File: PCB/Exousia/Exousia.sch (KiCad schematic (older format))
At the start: 3 parts

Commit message: added more stuff
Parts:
- added C? (x7): C, symbol Device:C
- added C? (x2): CP1, symbol Device:CP1
- added J?: I2C buss, symbol Connector:Conn_01x04_Female
- added L?: L, symbol Device:L
- added Q? (x4): Q_NMOS_DGS, symbol Device:Q_NMOS_DGS
- added R? (x2): 20m, symbol Device:R
- added R? (x8): R, symbol Device:R
- added R? (x4): 3.3K, symbol Device:R
- added TP?: FRWPG, symbol Connector:TestPoint
- added TP?: RVSPG, symbol Connector:TestPoint
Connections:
- net GND: now reaches J?.1 (Pin_1)
- net GND: now also J?.1 (Pin_1), U?.25 (ADDR0), U?.32 (ADDR1), C?.2, C?.2, C?.2, C?.2, C?.2, J?.1 (Pin_1), Q?.3 (S), Q?.3 (S), R?.1, R?.1
- net at J?.2 (Pin_2): now also U?.13 (ADPS), R?.2, R?.2, R?.2
- net at J?.2 (Pin_2): now also C?.1, C?.1, R?.1, R?.2, R?.2
- net at U?.1 (CSON): now also C?.1, R?.1
- net at U?.10 (PHASE1): now also C?.1, L?.1, Q?.1 (D), Q?.3 (S)
- net at U?.11 (UGATE1): now also Q?.2 (G)
- net at U?.12 (BOOT1): now also C?.2
- net at U?.14 (CSIN): now also C?.1, R?.1
- net at U?.15 (CSIP): now also C?.2, R?.1
- net at U?.16 (ADP): now also R?.1, R?.2
- net at U?.2 (CSOP): now also C?.2, R?.1
- net SDA: now reaches U?.21 (SDA)
- net SDA: now also J?.3 (Pin_3), R?.2
- net SCL: now reaches U?.22 (SCL)
- net SCL: now also J?.2 (Pin_2), R?.2
- net at U?.24 (FRWPG): now also R?.2, TP?.1
- net at U?.26 (RVSPG): now also R?.2, TP?.1
- net at U?.29 (REF): now also C?.1
- net at U?.3 (VOUTS): now also R?.1, R?.2
- net at U?.31 (VOUT): now also Q?.1 (D), R?.2, R?.2
- net at U?.4 (BOOT2): now also C?.2
- net at U?.5 (UGATE2): now also Q?.2 (G)
- net at U?.6 (PHASE2): now also C?.1, L?.2, Q?.1 (D), Q?.3 (S)
- net at U?.7 (LGATE2): now also Q?.2 (G)
- net at U?.9 (LGATE1): now also Q?.2 (G)
- new net: C?.1, C?.1, Q?.1 (D), R?.1, R?.2
- new net +3V3: J?.4 (Pin_4), R?.1, R?.1, R?.1, R?.1
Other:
- moved on the sheet: J?

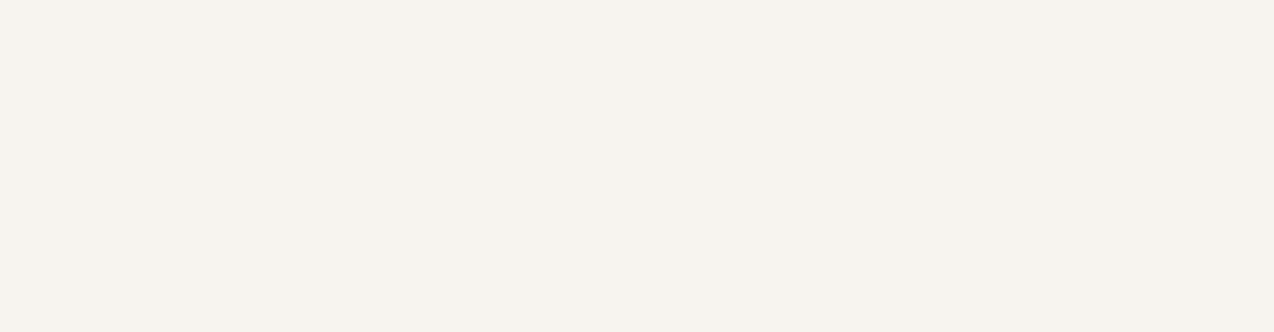
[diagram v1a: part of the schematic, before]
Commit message: added refrence design files
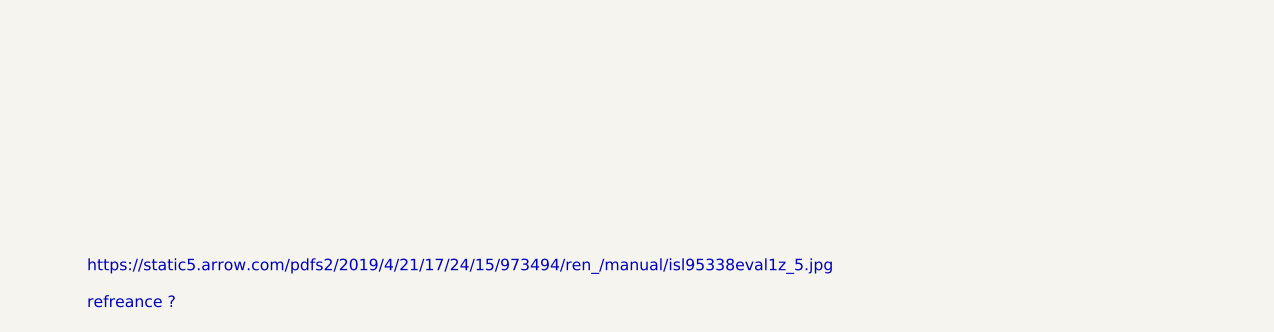
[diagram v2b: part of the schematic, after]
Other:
- note added: "https://static5.arrow.com/pdfs2/2019/4/21/17/24/15/973494/ren_/manual/isl95338eval1z_5.jpg\n\nrefreance ?"
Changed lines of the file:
@@
 Wire Wire Line
 	9300 1350 9350 1350
+Text Notes 1400 6900 0    50   ~ 0
+https://static5.arrow.com/pdfs2/2019/4/21/17/24/15/973494/ren_/manual/isl95338eval1z_5.jpg\n\nrefreance ?
 $EndSCHEMATC

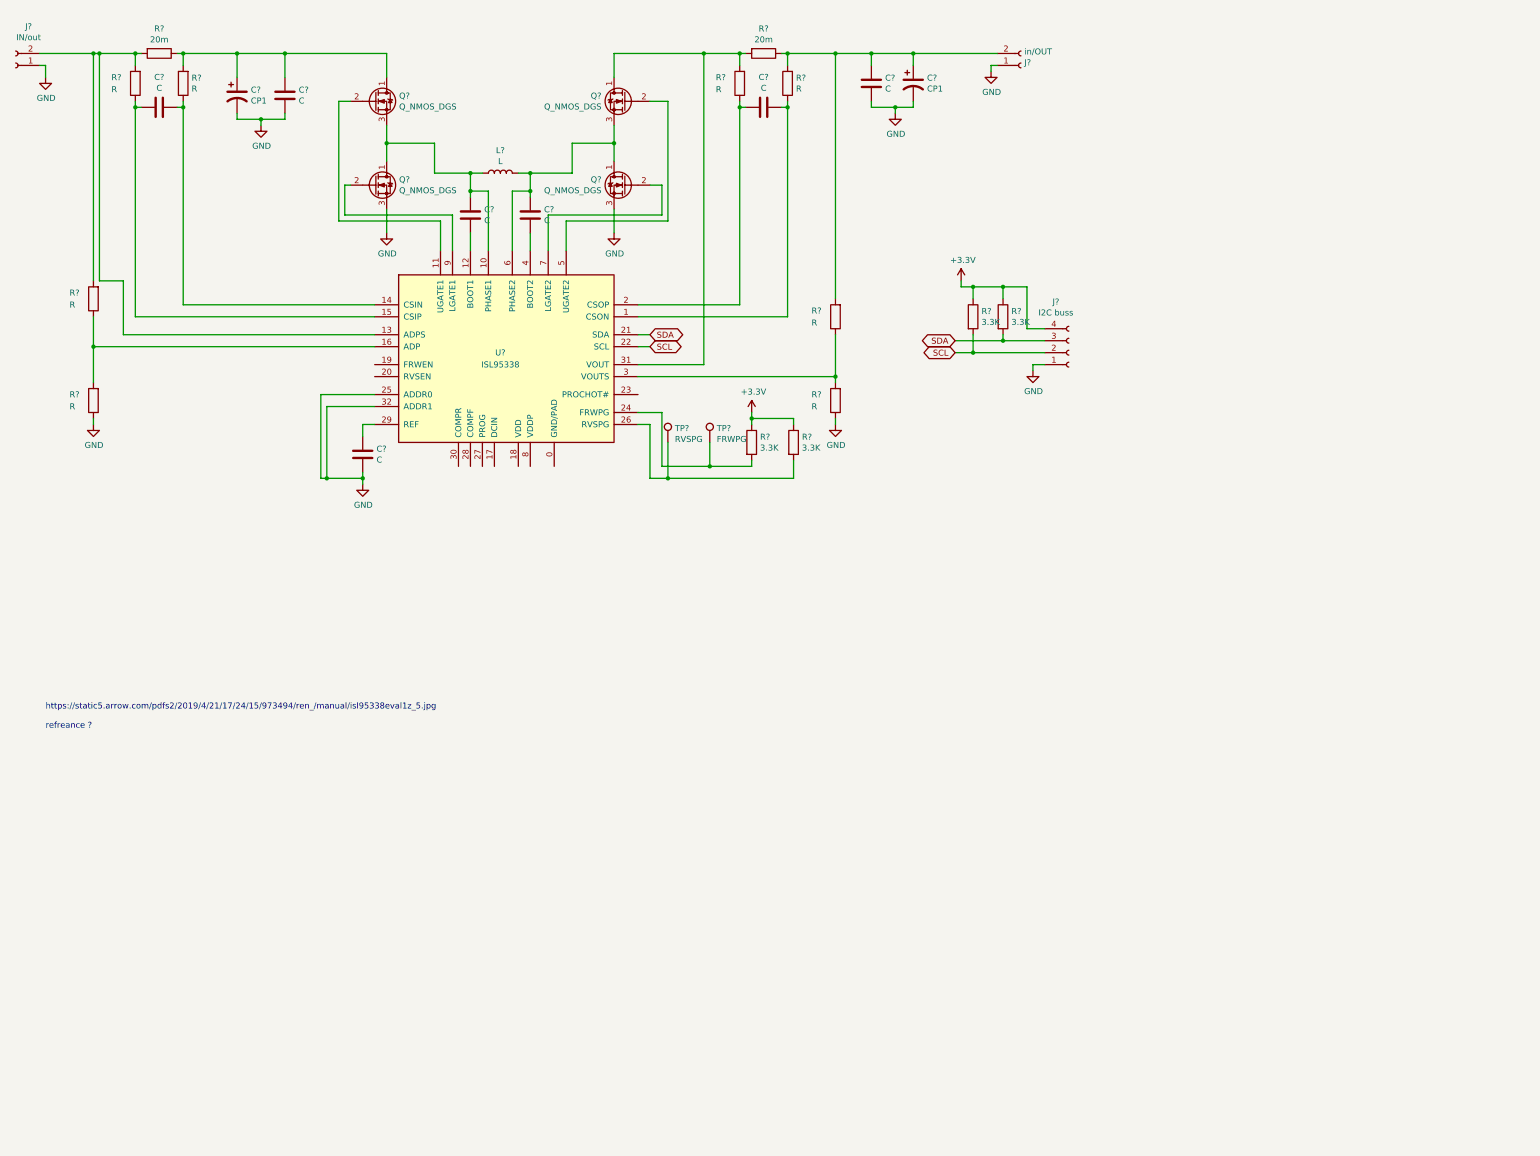
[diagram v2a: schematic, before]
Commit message: added nice FETs and more detailed circuti diogram
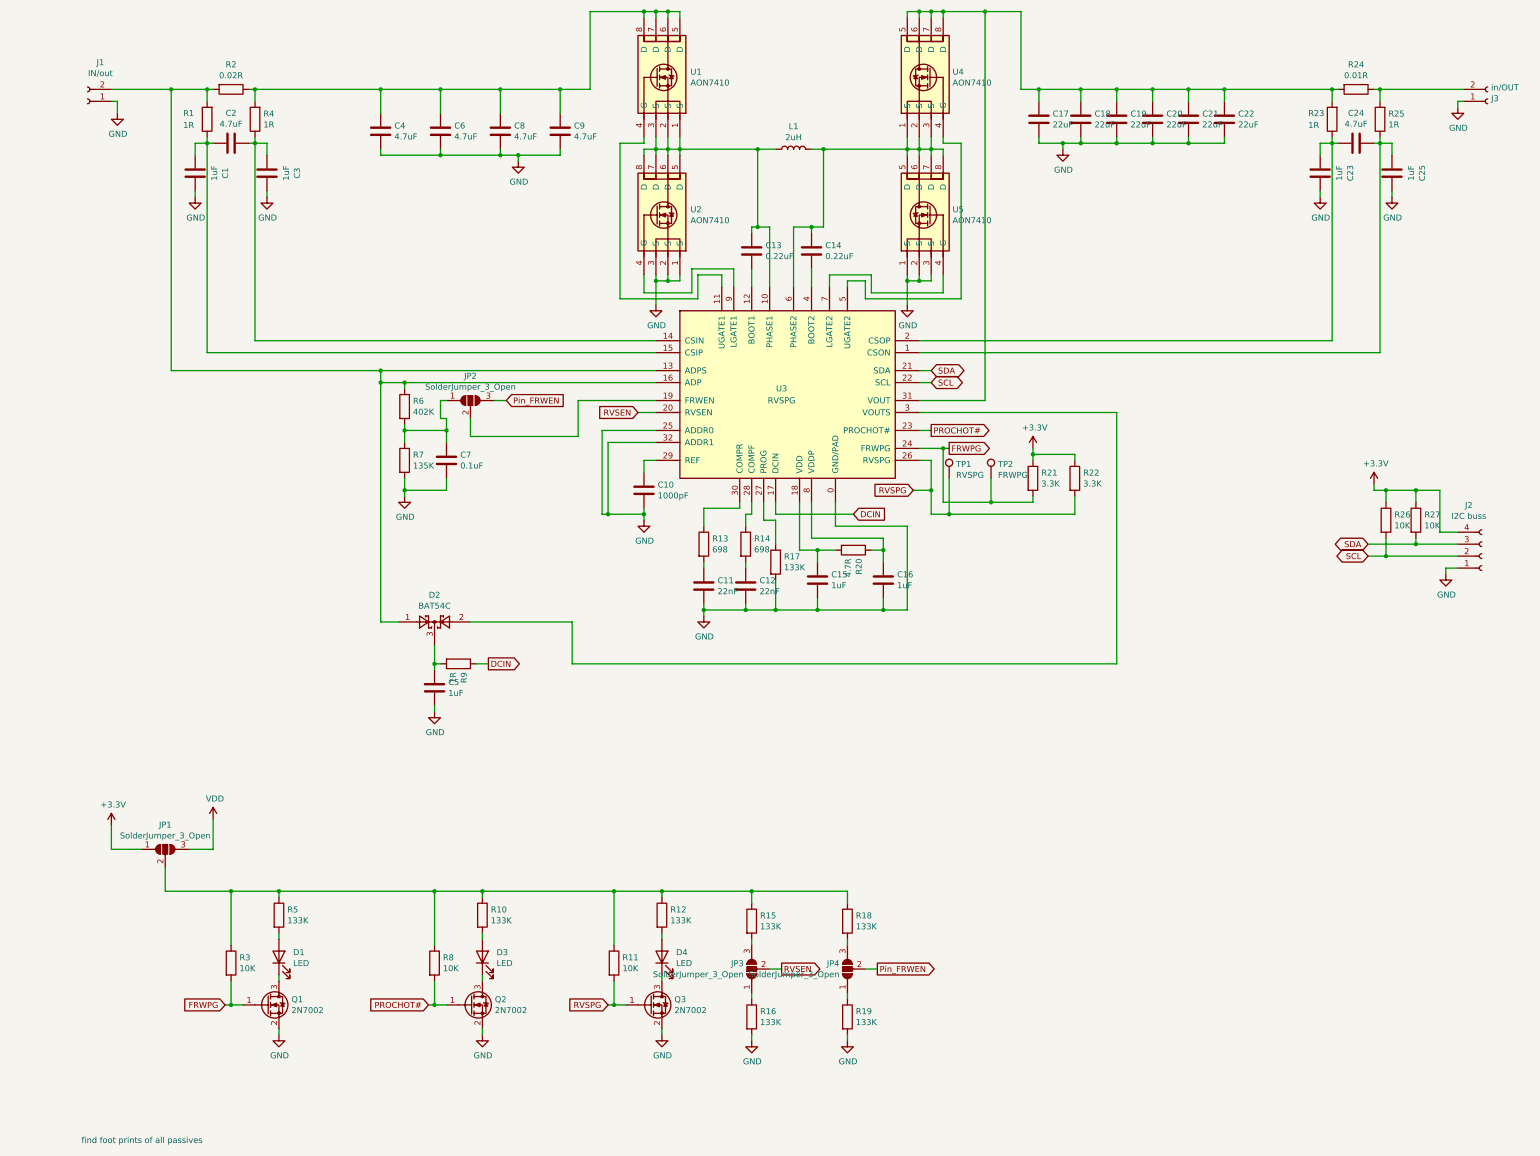
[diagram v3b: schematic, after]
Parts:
- removed C?: C, symbol Device:C
- removed C? (x2): CP1, symbol Device:CP1
- removed Q? (x4): Q_NMOS_DGS, symbol Device:Q_NMOS_DGS
- removed R? (x4): R, symbol Device:R
- added C1, C15, C16, C23, C25, C3, C5: 1uF, symbol Device:C
- added C11, C12: 22nF, symbol Device:C
- added C18, C19, C20, C21, C22: 22uF, symbol Device:C
- added C4, C6, C8, C9: 4.7uF, symbol Device:C
- added C7: 0.1uF, symbol Device:C
- added D1, D3, D4: LED, symbol Device:LED
- added D2: BAT54C, Package_TO_SOT_SMD:SOT-23, symbol Diode:BAT54C
- added JP1, JP2, JP3, JP4: SolderJumper_3_Open, symbol Jumper:SolderJumper_3_Open
- added Q1, Q2, Q3: 2N7002, Package_TO_SOT_SMD:SOT-23, symbol Transistor_FET:2N7002
- added R10, R12, R15, R16, R17, R18, R19, R5: 133K, symbol Device:R
- added R11, R3, R8: 10K, symbol Device:R
- added R13, R14: 698, symbol Device:R
- added R20: 4.7R, symbol Device:R
- added R6: 402K, symbol Device:R
- added R7: 135K, symbol Device:R
- added R9: 1R, symbol Device:R
- added U1, U2, U4, U5: AON7410, Package_DFN_QFN:DFN-6-1EP_3x3mm_P1mm_EP1.5x2.4mm, symbol AON7410:AON7410
- C10: renamed from C?; value C -> 1000pF
- C13, C14: renamed from C?; value C -> 0.22uF
- C17: renamed from C?; value C -> 22uF
- C2, C24: renamed from C?; value C -> 4.7uF
- L1: renamed from L?; value L -> 2uH
- R1, R23, R25, R4: renamed from R?; value R -> 1R
- R2: renamed from R?; value 20m -> 0.02R
- R24: renamed from R?; value 20m -> 0.01R
- R26, R27: renamed from R?; value 3.3K -> 10K
- U3: renamed from U?; value ISL95338 -> RVSPG
- gave numbers to parts that had none: 7
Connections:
- net +3V3: now also JP1.1 (A)
- net GND: now also U3.0 (GND/PAD), C1.1, C11.2, C12.2, C15.2, C16.2, C18.2, C19.2, C20.2, C21.2, C22.2, C23.1, C25.1, C3.1, C4.2, C5.2, C6.2, C7.2, C8.2, C9.2, Q1.2 (S), Q2.2 (S), Q3.2 (S), R16.2, R17.2, R19.2, R7.2, U2.1 (S), U2.2 (S), U2.3 (S), U5.1 (S), U5.2 (S), U5.3 (S)
- net at J1.2 (Pin_2), R1.2, R2.2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: now also U3.16 (ADP), D2.1, R6.1
- net at J3.2 (Pin_2), R24.1, R25.2: no longer C17.1
- net at C24.1, R25.1, U3.1 (CSON): now also C25.2
- net at C13.1, L1.1, U3.10 (PHASE1): now also U1.1 (S), U1.2 (S), U1.3 (S), U2.5 (D), U2.6 (D), U2.7 (D), U2.8 (D)
- net at U3.11 (UGATE1): now also U1.4 (G)
- net at C2.1, R4.1, U3.14 (CSIN): now also C3.2
- net at C2.2, R1.1, U3.15 (CSIP): now also C1.2
- net DCIN: now reaches U3.17 (DCIN)
- net DCIN: now also R9.1
- net at U3.18 (VDD): now also C15.1, R20.2
- net at U3.19 (FRWEN): now also JP2.2 (C)
- net at C24.2, R23.1, U3.2 (CSOP): now also C23.2
- net RVSEN: now reaches U3.20 (RVSEN)
- net RVSEN: now also JP3.2 (C)
- net PROCHOT#: now reaches U3.23 (PROCHOT#)
- net PROCHOT#: now also Q2.1 (G), R8.2
- net FRWPG: now reaches R21.2, TP2.1, U3.24 (FRWPG)
- net FRWPG: now also Q1.1 (G), R3.2
- net RVSPG: now reaches R22.2, TP1.1, U3.26 (RVSPG)
- net RVSPG: now also Q3.1 (G), R11.2
- net at U3.27 (PROG): now also R17.1
- net at U3.28 (COMPF): now also R14.1
- net at U3.3 (VOUTS): now also D2.2
- net at U3.30 (COMPR): now also R13.1
- net at R23.2, R24.2, U3.31 (VOUT): now also C17.1, C18.1, C19.1, C20.1, C21.1, C22.1, U4.5 (D), U4.6 (D), U4.7 (D), U4.8 (D)
- net at U3.5 (UGATE2): now also U4.4 (G)
- net at C14.1, L1.2, U3.6 (PHASE2): now also U4.1 (S), U4.2 (S), U4.3 (S), U5.5 (D), U5.6 (D), U5.7 (D), U5.8 (D)
- net at U3.7 (LGATE2): now also U5.4 (G)
- net at U3.8 (VDDP): now also C16.1, R20.1
- net at U3.9 (LGATE1): now also U2.4 (G)
- net at R2.1, R4.2: now also C4.1, C6.1, C8.1, C9.1, U1.5 (D), U1.6 (D), U1.7 (D), U1.8 (D)
- new net: C11.1, R13.2
- new net: C12.1, R14.2
- new net: D1.1 (K), Q1.3 (D)
- new net: D1.2 (A), R5.2
- new net: JP1.2 (C), R10.1, R11.1, R12.1, R15.1, R18.1, R3.1, R5.1, R8.1
- new net: D3.1 (K), Q2.3 (D)
- new net: D3.2 (A), R10.2
- new net: D4.1 (K), Q3.3 (D)
- new net: D4.2 (A), R12.2
- new net: C5.1, D2.3, R9.2
- new net: C7.1, JP2.1 (A), R6.2, R7.1
- new net: JP3.1 (A), R16.1
- new net: JP3.3 (B), R15.2
- new net: JP4.1 (A), R19.1
- new net: JP4.3 (B), R18.2
- new net Pin_FRWEN: JP2.3 (B), JP4.2 (C)
- new net VDD: JP1.3 (B)
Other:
- note added: "find foot prints of all passives \n\n"
- note removed: "https://static5.arrow.com/pdfs2/2019/4/21/17/24/15/973494/ren_/manual/isl95338eval1z_5.jpg\n\nrefreance ?"
- moved on the sheet: C10, C13, C14, C17, C2, C24, J1, J2, J3, L1, R1, R2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

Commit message: started adding footprints to all the components!
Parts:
- C1, C10, C11, C12, C13, C14, C15, C16, C2, C3: footprint (none) -> Capacitor_SMD:C_0603_1608Metric
- C17, C4, C6, C8, C9: footprint (none) -> Capacitor_SMD:C_0805_2012Metric
- R26, R27: footprint (none) -> Resistor_SMD:R_0603_1608Metric
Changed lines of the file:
@@
 F 0 "C10" H 6515 4946 50  0000 L CNN
 F 1 "1000pF" H 6515 4855 50  0000 L CNN
-F 2 "" H 6438 4750 50  0001 C CNN
+F 2 "Capacitor_SMD:C_0603_1608Metric" H 6438 4750 50  0001 C CNN
 F 3 "~" H 6400 4900 50  0001 C CNN
 	1    6400 4900
@@
 F 0 "C13" H 7415 2946 50  0000 L CNN
 F 1 "0.22uF" H 7415 2855 50  0000 L CNN
-F 2 "" H 7338 2750 50  0001 C CNN
+F 2 "Capacitor_SMD:C_0603_1608Metric" H 7338 2750 50  0001 C CNN
 F 3 "~" H 7300 2900 50  0001 C CNN
 	1    7300 2900
@@
 F 0 "C14" H 7915 2946 50  0000 L CNN
 F 1 "0.22uF" H 7915 2855 50  0000 L CNN
-F 2 "" H 7838 2750 50  0001 C CNN
+F 2 "Capacitor_SMD:C_0603_1608Metric" H 7838 2750 50  0001 C CNN
 F 3 "~" H 7800 2900 50  0001 C CNN
 	1    7800 2900
@@
 F 0 "C17" H 9815 1846 50  0000 L CNN
 F 1 "22uF" H 9815 1755 50  0000 L CNN
-F 2 "" H 9738 1650 50  0001 C CNN
+F 2 "Capacitor_SMD:C_0805_2012Metric" H 9738 1650 50  0001 C CNN
 F 3 "~" H 9700 1800 50  0001 C CNN
 	1    9700 1800
@@
 F 0 "C2" V 2698 2000 50  0000 C CNN
 F 1 "4.7uF" V 2789 2000 50  0000 C CNN
-F 2 "" H 2988 1850 50  0001 C CNN
+F 2 "Capacitor_SMD:C_0603_1608Metric" H 2988 1850 50  0001 C CNN
 F 3 "~" H 2950 2000 50  0001 C CNN
 	1    2950 2000
@@
 F 0 "R27" H 12920 5196 50  0000 L CNN
 F 1 "10K" H 12920 5105 50  0000 L CNN
-F 2 "" V 12780 5150 50  0001 C CNN
+F 2 "Resistor_SMD:R_0603_1608Metric" V 12780 5150 50  0001 C CNN
 F 3 "~" H 12850 5150 50  0001 C CNN
 	1    12850 5150
@@
 F 0 "R26" H 12670 5196 50  0000 L CNN
 F 1 "10K" H 12670 5105 50  0000 L CNN
-F 2 "" V 12530 5150 50  0001 C CNN
+F 2 "Resistor_SMD:R_0603_1608Metric" V 12530 5150 50  0001 C CNN
 F 3 "~" H 12600 5150 50  0001 C CNN
 	1    12600 5150
@@
 F 0 "C4" H 4315 1946 50  0000 L CNN
 F 1 "4.7uF" H 4315 1855 50  0000 L CNN
-F 2 "" H 4238 1750 50  0001 C CNN
+F 2 "Capacitor_SMD:C_0805_2012Metric" H 4238 1750 50  0001 C CNN
 F 3 "~" H 4200 1900 50  0001 C CNN
 	1    4200 1900
@@
 F 0 "C6" H 4815 1946 50  0000 L CNN
 F 1 "4.7uF" H 4815 1855 50  0000 L CNN
-F 2 "" H 4738 1750 50  0001 C CNN
+F 2 "Capacitor_SMD:C_0805_2012Metric" H 4738 1750 50  0001 C CNN
 F 3 "~" H 4700 1900 50  0001 C CNN
 	1    4700 1900
@@
 F 0 "C8" H 5315 1946 50  0000 L CNN
 F 1 "4.7uF" H 5315 1855 50  0000 L CNN
-F 2 "" H 5238 1750 50  0001 C CNN
+F 2 "Capacitor_SMD:C_0805_2012Metric" H 5238 1750 50  0001 C CNN
 F 3 "~" H 5200 1900 50  0001 C CNN
 	1    5200 1900
@@
 F 0 "C9" H 5815 1946 50  0000 L CNN
 F 1 "4.7uF" H 5815 1855 50  0000 L CNN
-F 2 "" H 5738 1750 50  0001 C CNN
+F 2 "Capacitor_SMD:C_0805_2012Metric" H 5738 1750 50  0001 C CNN
 F 3 "~" H 5700 1900 50  0001 C CNN
 	1    5700 1900
@@
 F 0 "C3" V 2998 2250 50  0000 C CNN
 F 1 "1uF" V 3089 2250 50  0000 C CNN
-F 2 "" H 3288 2100 50  0001 C CNN
+F 2 "Capacitor_SMD:C_0603_1608Metric" H 3288 2100 50  0001 C CNN
 F 3 "~" H 3250 2250 50  0001 C CNN
 	1    3250 2250
@@
 F 0 "C1" V 2398 2250 50  0000 C CNN
 F 1 "1uF" V 2489 2250 50  0000 C CNN
-F 2 "" H 2688 2100 50  0001 C CNN
+F 2 "Capacitor_SMD:C_0603_1608Metric" H 2688 2100 50  0001 C CNN
 F 3 "~" H 2650 2250 50  0001 C CNN
 	1    2650 2250
@@
 F 0 "C11" H 7015 5746 50  0000 L CNN
 F 1 "22nF" H 7015 5655 50  0000 L CNN
-F 2 "" H 6938 5550 50  0001 C CNN
+F 2 "Capacitor_SMD:C_0603_1608Metric" H 6938 5550 50  0001 C CNN
 F 3 "~" H 6900 5700 50  0001 C CNN
 	1    6900 5700
@@
 F 0 "C12" H 7365 5746 50  0000 L CNN
 F 1 "22nF" H 7365 5655 50  0000 L CNN
-F 2 "" H 7288 5550 50  0001 C CNN
+F 2 "Capacitor_SMD:C_0603_1608Metric" H 7288 5550 50  0001 C CNN
 F 3 "~" H 7250 5700 50  0001 C CNN
 	1    7250 5700
@@
 F 0 "C15" H 7965 5696 50  0000 L CNN
 F 1 "1uF" H 7965 5605 50  0000 L CNN
-F 2 "" H 7888 5500 50  0001 C CNN
+F 2 "Capacitor_SMD:C_0603_1608Metric" H 7888 5500 50  0001 C CNN
 F 3 "~" H 7850 5650 50  0001 C CNN
 	1    7850 5650
@@
 F 0 "C16" H 8515 5696 50  0000 L CNN
 F 1 "1uF" H 8515 5605 50  0000 L CNN
-F 2 "" H 8438 5500 50  0001 C CNN
+F 2 "Capacitor_SMD:C_0603_1608Metric" H 8438 5500 50  0001 C CNN
 F 3 "~" H 8400 5650 50  0001 C CNN
 	1    8400 5650

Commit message: done all but 1 footprints
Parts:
- C18, C19, C20, C21, C22: footprint (none) -> Capacitor_SMD:C_0805_2012Metric
- C23, C24, C25, C5, C7: footprint (none) -> Capacitor_SMD:C_0603_1608Metric
- D1, D3, D4: footprint (none) -> LED_SMD:LED_1206_3216Metric
- J1, J2: footprint (none) -> Connector_PinSocket_2.54mm:PinSocket_1x04_P2.54mm_Vertical
- J3: footprint (none) -> Connector_PinSocket_2.54mm:PinSocket_1x02_P2.54mm_Vertical
- JP1, JP2, JP3, JP4: footprint (none) -> Connector_PinSocket_2.54mm:PinSocket_1x03_P2.54mm_Vertical
- R1, R10, R11, R12, R13, R14, R15, R16, R17, R18, R19, R20, R21, R22, R23, R25, R3, R4, R5, R6, R7, R8, R9: footprint (none) -> Resistor_SMD:R_0603_1608Metric
- R2, R24: footprint (none) -> Resistor_SMD:R_1206_3216Metric
- TP1, TP2: footprint (none) -> TestPoint:TestPoint_Loop_D2.50mm_Drill1.0mm
- U3: footprint (none) -> Package_DFN_QFN:TQFN-24-1EP_4x4mm_P0.5mm_EP2.8x2.8mm_PullBack
